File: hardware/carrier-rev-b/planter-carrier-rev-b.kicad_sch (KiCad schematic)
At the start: 20 parts, among them J1 PROTECTED BATTERY, J2 MOISTURE PROBE, J3 WEACT 1.54 INCH, J4 XIAO BAT LEADS, Q1 AO3401A, U1 Seeed XIAO ESP32-C6 or ESP32-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

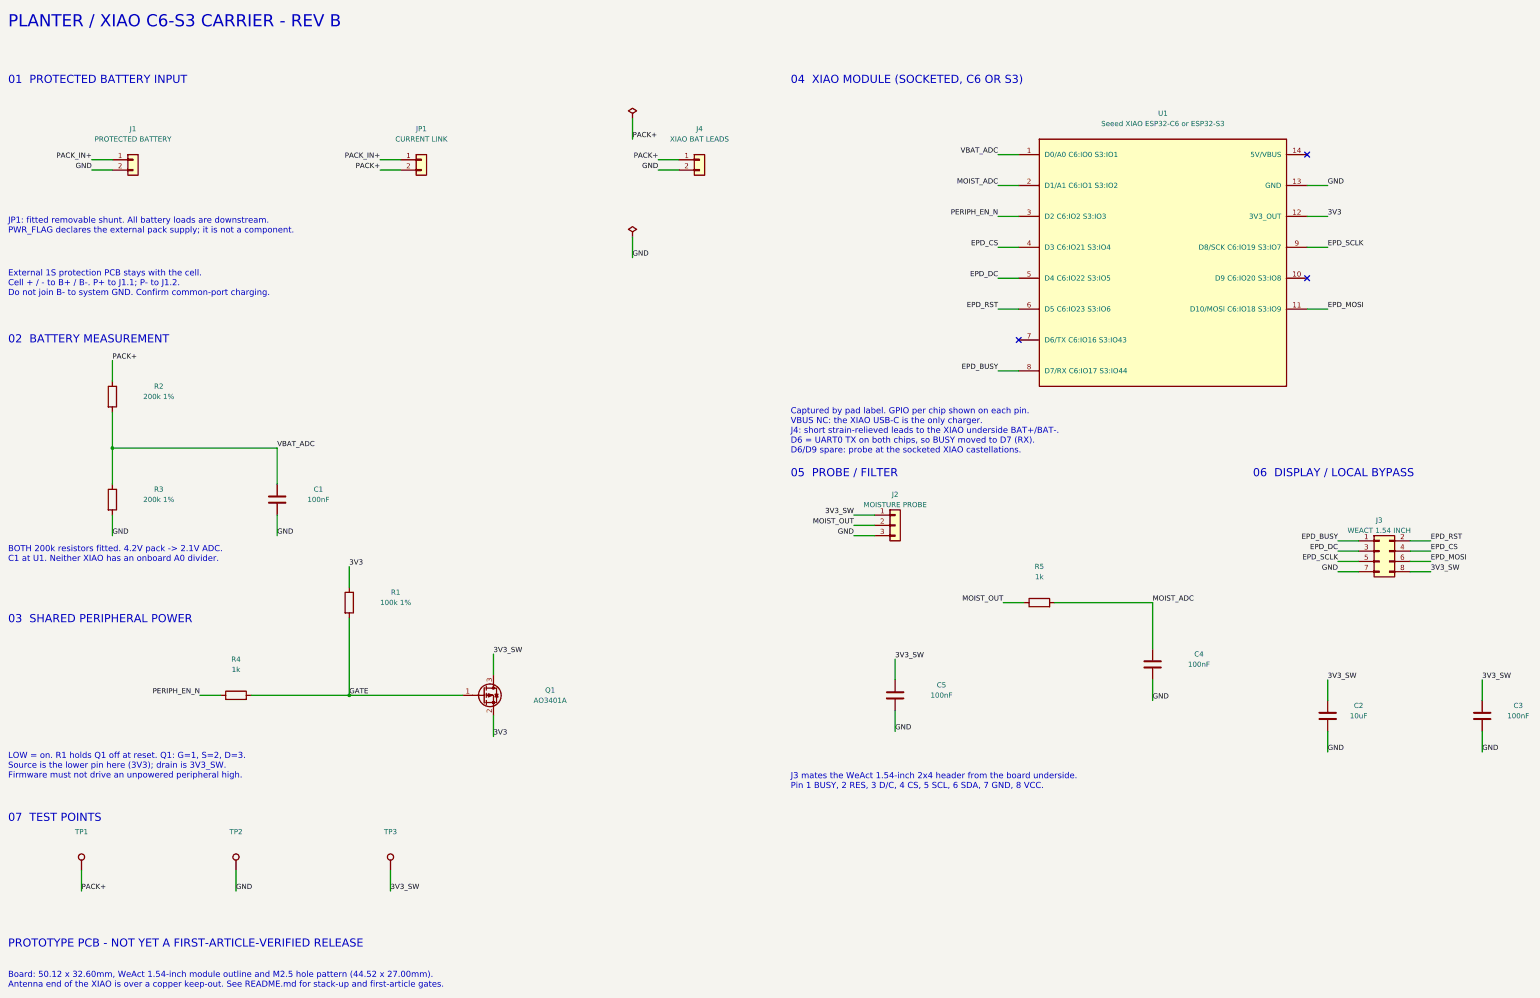
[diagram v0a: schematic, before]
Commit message: Rev B carrier: add DW01A/FS8205A protection, drop antenna keep-out, JLCPCB-ready fab
- Battery protection on board: DW01A (U2) + FS8205A (Q2), low-side,
  with R6 100R / C6 100nF supply and R7 1k on VM/CS. GND is now the
  protected pack negative; the cell's negative is PACK_IN-. Charging
  stays with the XIAO (USB-C only).
- Antenna keep-out removed: the board uses an external U.FL antenna, so
  the ground pour runs under the whole module. README says how to
  select the U.FL on the C6.
- LCSC part numbers on every machine-placeable part.
- make_fab.sh: JLCPCB BOM with every designator listed in full (no
  ranges), a separate full BOM including the hand-fitted parts, and a
  top-side CPL in JLCPCB's column names, filtered to the BOM's parts.
- Silkscreen raised to JLCPCB's legend minimums (1.0 mm text,
  0.15 mm lines), labels moved clear of each other and the stitching
  vias. Copper, mask, paste, outline and drills are unchanged by this.
- ERC, DRC (including warnings) and schematic parity all clean.

Co-Authored-By: Claude Opus 5.5 <noreply@anthropic.com>
Claude-Session: https://claude.ai/code/session_01AZKEkQvxhWy7uorWE2pBMp
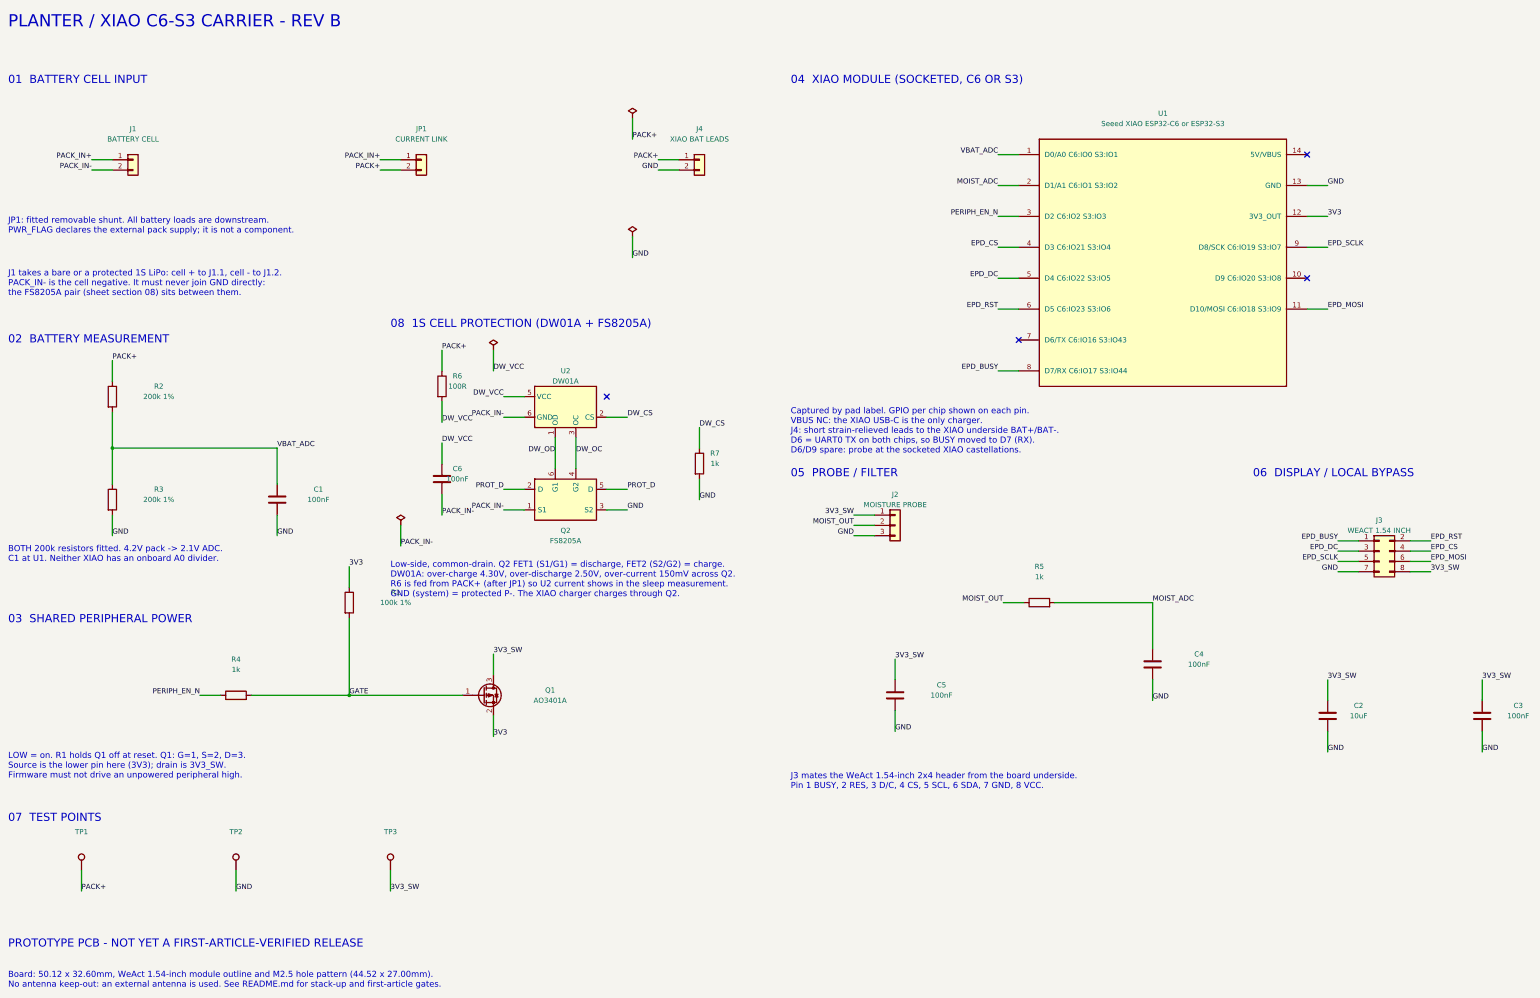
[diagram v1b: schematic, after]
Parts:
- added C6: 100nF, Capacitor_SMD:C_0603_1608Metric, symbol Planter:C
- added Q2: FS8205A, Package_TO_SOT_SMD:SOT-23-6, symbol Planter:FS8205A_SOT23-6
- added R6: 100R, Resistor_SMD:R_0603_1608Metric, symbol Planter:R
- added R7: 1k, Resistor_SMD:R_0603_1608Metric, symbol Planter:R
- added U2: DW01A, Package_TO_SOT_SMD:SOT-23-6, symbol Planter:DW01A
- C1, C3, C4, C5: LCSC (none) -> C14663
- C2: LCSC (none) -> C15850
- J1: value PROTECTED BATTERY -> BATTERY CELL; LCSC (none) -> C173752
- J2: LCSC (none) -> C157929
- Q1: LCSC (none) -> C15127
- R1: LCSC (none) -> C25803
- R2, R3: LCSC (none) -> C25811
- R4, R5: LCSC (none) -> C21190
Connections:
- net GND: now also Q2.3 (S2), R7.2; no longer J1.2 (Pin_2)
- net PACK+: now also R6.1
- new net DW_CS: R7.1, U2.2 (CS)
- new net DW_OC: Q2.4 (G2), U2.3 (OC)
- new net DW_OD: Q2.6 (G1), U2.1 (OD)
- new net DW_VCC: C6.1, R6.2, U2.5 (VCC)
- new net PACK_IN-: C6.2, J1.2 (Pin_2), Q2.1 (S1), U2.6 (GND)
- new net PROT_D: Q2.2 (D), Q2.5 (D)
- no-connect marks 3 -> 4
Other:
- note added: "01 BATTERY CELL INPUT"
- note added: "08 1S CELL PROTECTION (DW01A + FS8205A)"
- note added: "Board: 50.12 x 32.60mm, WeAct 1.54-inch module outline and M2.5 hole pattern (44.52 x 27.00mm). No antenna keep-out: an external antenna is used. See README.md for stack-up and first-article gates."
- note added: "J1 takes a bare or a protected 1S LiPo: cell + to J1.1, cell - to J1.2. PACK_IN- is the cell negative. It must never join GND directly: the FS8205A pair (sheet section 08) sits between them."
- note added: "Low-side, common-drain. Q2 FET1 (S1/G1) = discharge, FET2 (S2/G2) = charge. DW01A: over-charge 4.30V, over-discharge 2.50V, over-current 150mV across Q2. R6 is fed from PACK+ (after JP1) so U2 current shows in the sleep measurement. GND (system) = protected P-. The XIAO charger charges through Q2."
- note removed: "01 PROTECTED BATTERY INPUT"
- note removed: "Board: 50.12 x 32.60mm, WeAct 1.54-inch module outline and M2.5 hole pattern (44.52 x 27.00mm). Antenna end of the XIAO is over a copper keep-out. See README.md for stack-up and first-article gates."
- note removed: "External 1S protection PCB stays with the cell. Cell + / - to B+ / B-. P+ to J1.1; P- to J1.2. Do not join B- to system GND. Confirm common-port charging."
